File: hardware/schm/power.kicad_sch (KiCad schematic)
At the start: 16 parts, among them J1 VBUS input fly-leads, U2 AP63205WU-7

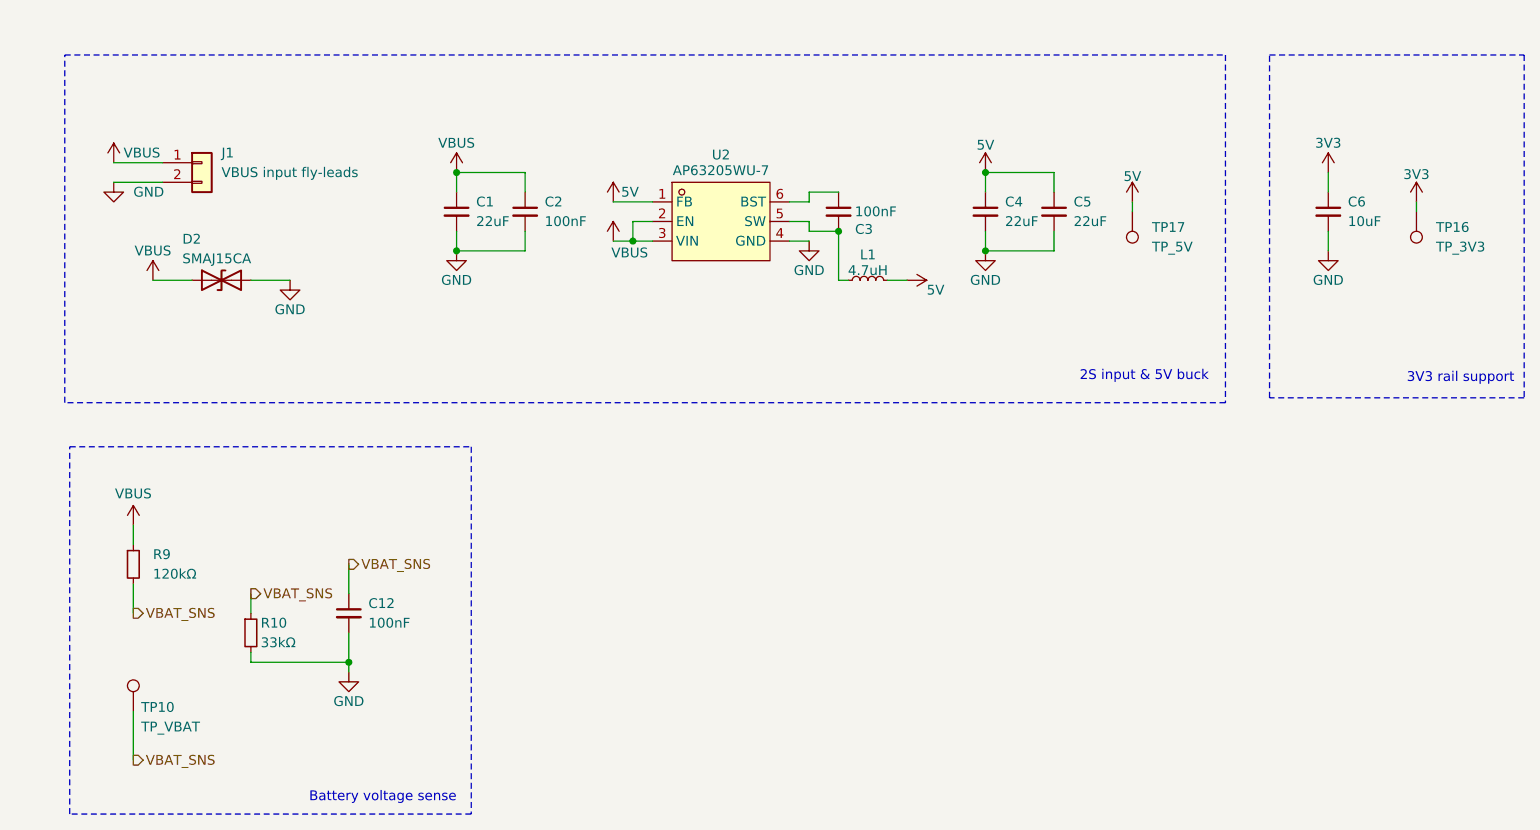
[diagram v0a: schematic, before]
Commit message: feat: organize subsheets
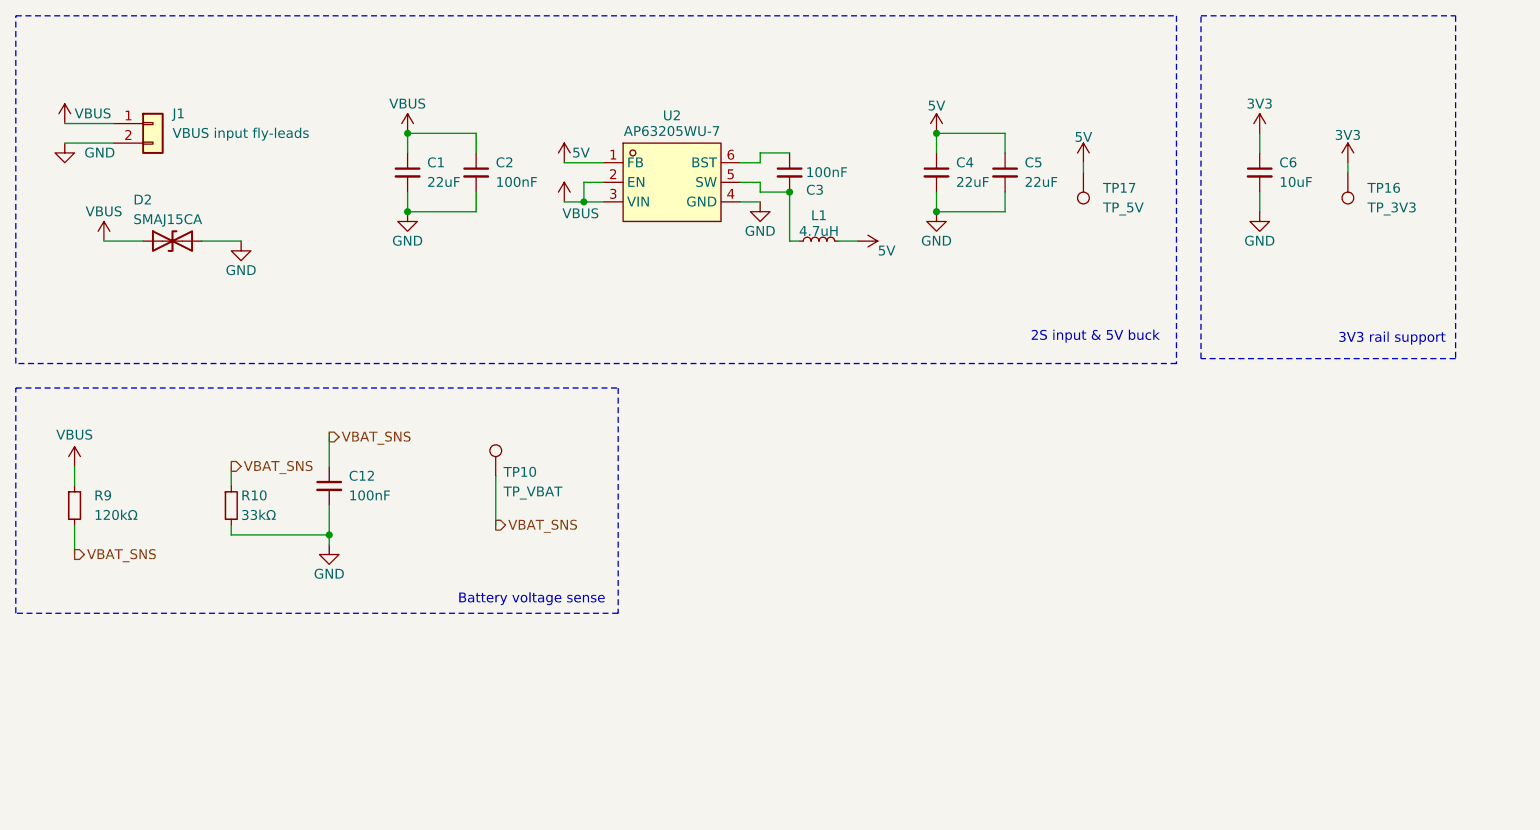
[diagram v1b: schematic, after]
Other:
- company: (none) -> Kieran Klukas
- title: (none) -> Holy Guacamole
- moved on the sheet: C1, C12, C2, C3, C4, C5, C6, D2, J1, L1, R10, R9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

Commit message: feat: organize into better sheets
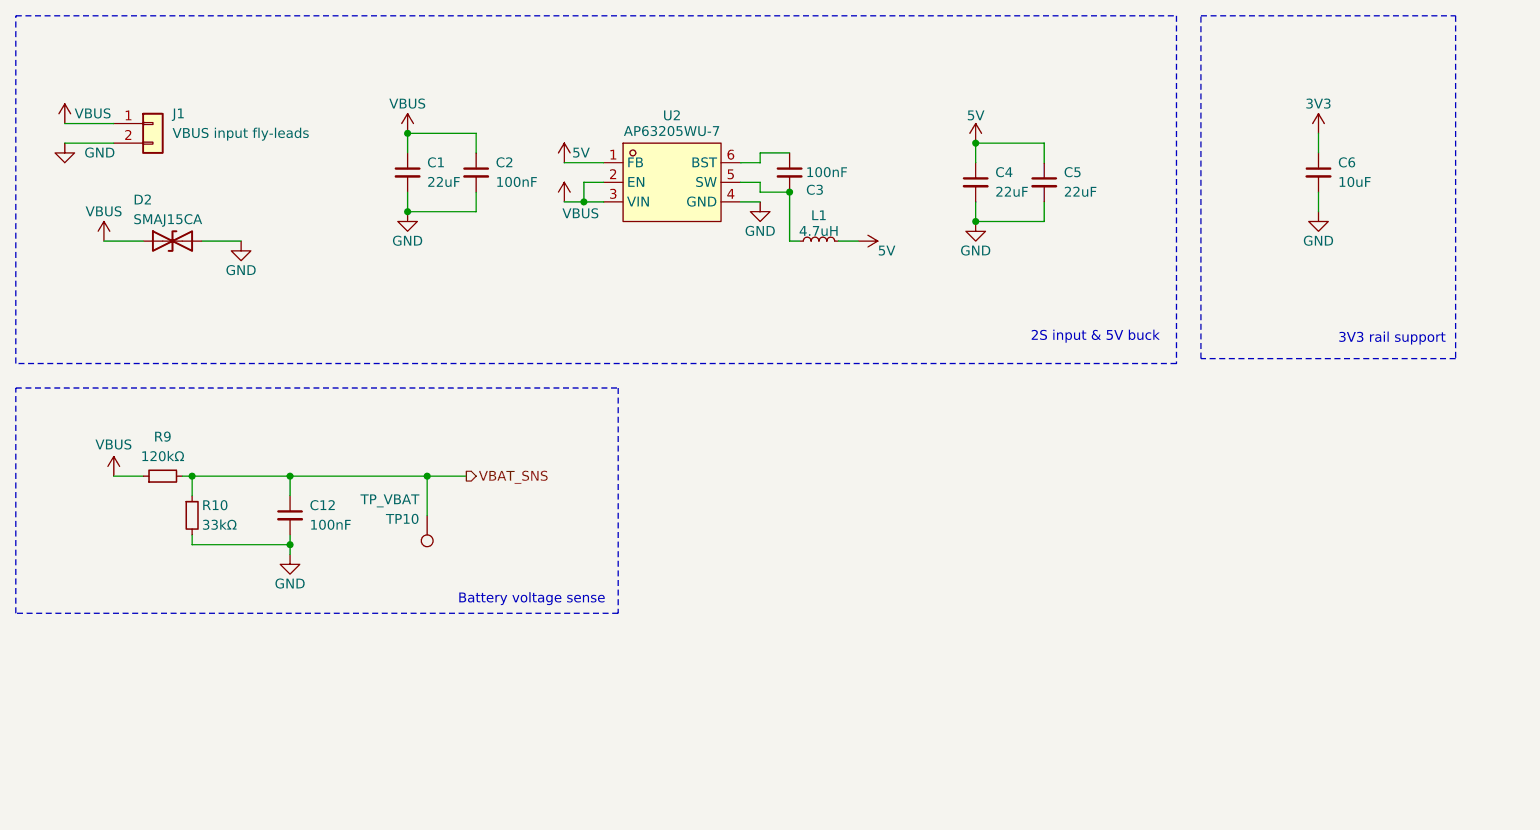
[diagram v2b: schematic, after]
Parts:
- removed TP16: TP_3V3, TestPoint:TestPoint_Pad_D1.0mm, symbol Connector:TestPoint
- removed TP17: TP_5V, TestPoint:TestPoint_Pad_D1.0mm, symbol Connector:TestPoint
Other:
- moved on the sheet: C12, C4, C5, C6, R10, TP10
